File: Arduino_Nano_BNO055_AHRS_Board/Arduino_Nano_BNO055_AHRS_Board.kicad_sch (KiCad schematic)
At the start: 7 parts, among them J1 Conn_01x04, J2 Conn_01x02_Socket, J3 Conn_01x07_Pin, J4 Conn_01x02_Pin, J5 Conn_01x02_Pin, J6 Conn_01x06_Pin

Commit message: Made one update that I didn't save ...
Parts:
- removed J2: Conn_01x02_Socket, Connector_PinSocket_2.54mm:PinSocket_1x02_P2.54mm_Vertical, symbol Connector:Conn_01x02_Socket
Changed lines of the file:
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@@
   (junction (at 91.44 91.44) (diameter 0) (color 0 0 0 0)
   )
-  (junction (at 69.85 151.13) (diameter 0) (color 0 0 0 0)
-  )
-  (junction (at 80.01 130.81) (diameter 0) (color 0 0 0 0)
-  )
   (junction (at 92.71 130.81) (diameter 0) (color 0 0 0 0)
   )
@@
     (stroke (width 0) (type default))
   )
-  (wire (pts (xy 69.85 139.7) (xy 80.01 139.7))
-    (stroke (width 0) (type default))
-  )
-  (wire (pts (xy 50.8 130.81) (xy 80.01 130.81))
-    (stroke (width 0) (type default))
-  )
   (wire (pts (xy 130.81 91.44) (xy 147.32 91.44))
     (stroke (width 0) (type default))
@@
     (stroke (width 0) (type default))
   )
-  (wire (pts (xy 80.01 130.81) (xy 92.71 130.81))
+  (wire (pts (xy 50.8 130.81) (xy 92.71 130.81))
     (stroke (width 0) (type default))
   )
@@
     (stroke (width 0) (type default))
   )
-  (wire (pts (xy 59.69 151.13) (xy 69.85 151.13))
+  (wire (pts (xy 59.69 151.13) (xy 83.82 151.13))
     (stroke (width 0) (type default))
   )
@@
     (stroke (width 0) (type default))
   )
-  (wire (pts (xy 69.85 142.24) (xy 69.85 151.13))
-    (stroke (width 0) (type default))
-  )
   (wire (pts (xy 83.82 133.35) (xy 90.17 133.35))
     (stroke (width 0) (type default))
@@
     (stroke (width 0) (type default))
   )
-  (wire (pts (xy 80.01 139.7) (xy 80.01 130.81))
-    (stroke (width 0) (type default))
-  )
   (wire (pts (xy 30.48 88.9) (xy 30.48 124.46))
     (stroke (width 0) (type default))
@@
   )
   (wire (pts (xy 38.1 88.9) (xy 38.1 99.06))
-    (stroke (width 0) (type default))
-  )
-  (wire (pts (xy 69.85 151.13) (xy 83.82 151.13))
     (stroke (width 0) (type default))
   )
@@
         )
       )
-    )
-  )
-  (symbol (lib_id "Connector:Conn_01x02_Socket") (at 64.77 142.24 180) (unit 1)
-    (in_bom yes) (on_board yes) (dnp no) (fields_autoplaced)
-    (property "Reference" "J2" (at 65.405 135.89 0)
-      (effects (font (size 1.27 1.27)))
-    )
-    (property "Value" "Conn_01x02_Socket" (at 65.405 138.43 0)
-      (effects (font (size 1.27 1.27)))
-    )
-    (property "Footprint" "Connector_PinSocket_2.54mm:PinSocket_1x02_P2.54mm_Vertical" (at 64.77 142.24 0)
-      (effects (font (size 1.27 1.27)) hide)
-    )
-    (property "Datasheet" "~" (at 64.77 142.24 0)
-      (effects (font (size 1.27 1.27)) hide)
-    )
-    (pin "1")
-    (pin "2")
-    (instances
-      (project "Arduino_Nano_BNO055_AHRS_Board"
-        (path "/26c454b3-0fc6-4f29-b44e-9912b5b9bb77"
-          (reference "J2") (unit 1)
-        )
-      )

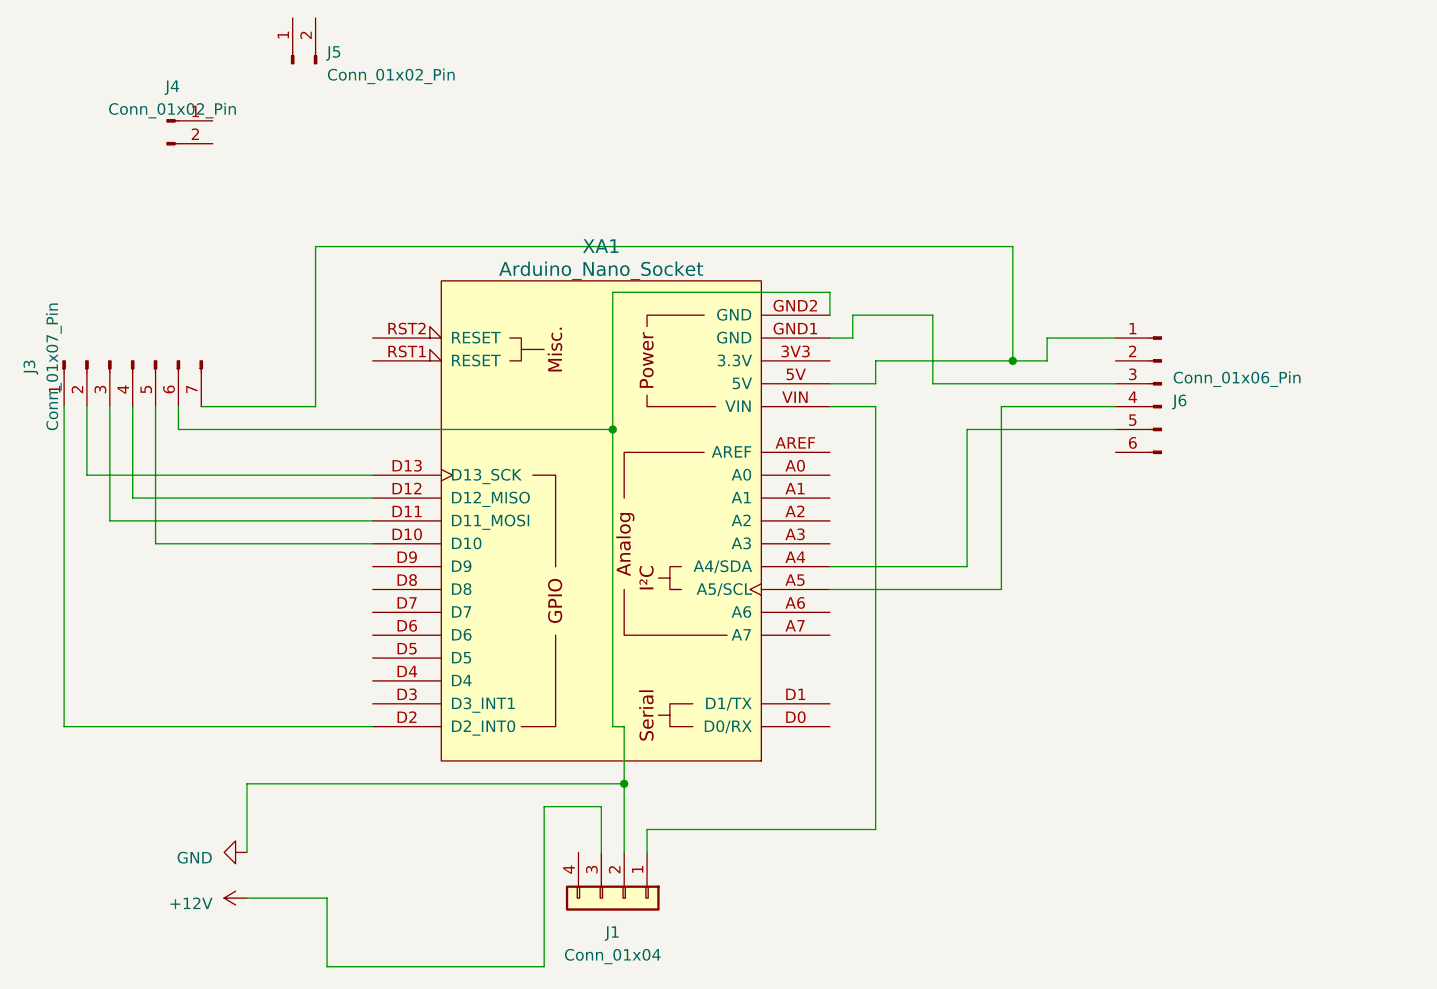
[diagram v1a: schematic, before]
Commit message: Updates Arduino_Nano_BNO055_AHRS_Board files. The older version required a via to cross two traces. This new version uses a larger PCB blank (one-sided) and no longer requires any vias. I also moved the BNO055 sensor away from the buck power converter (and all the other electronics on the board) to help minimize EMI, which can make it hard for the Magnetometer to calibrate.
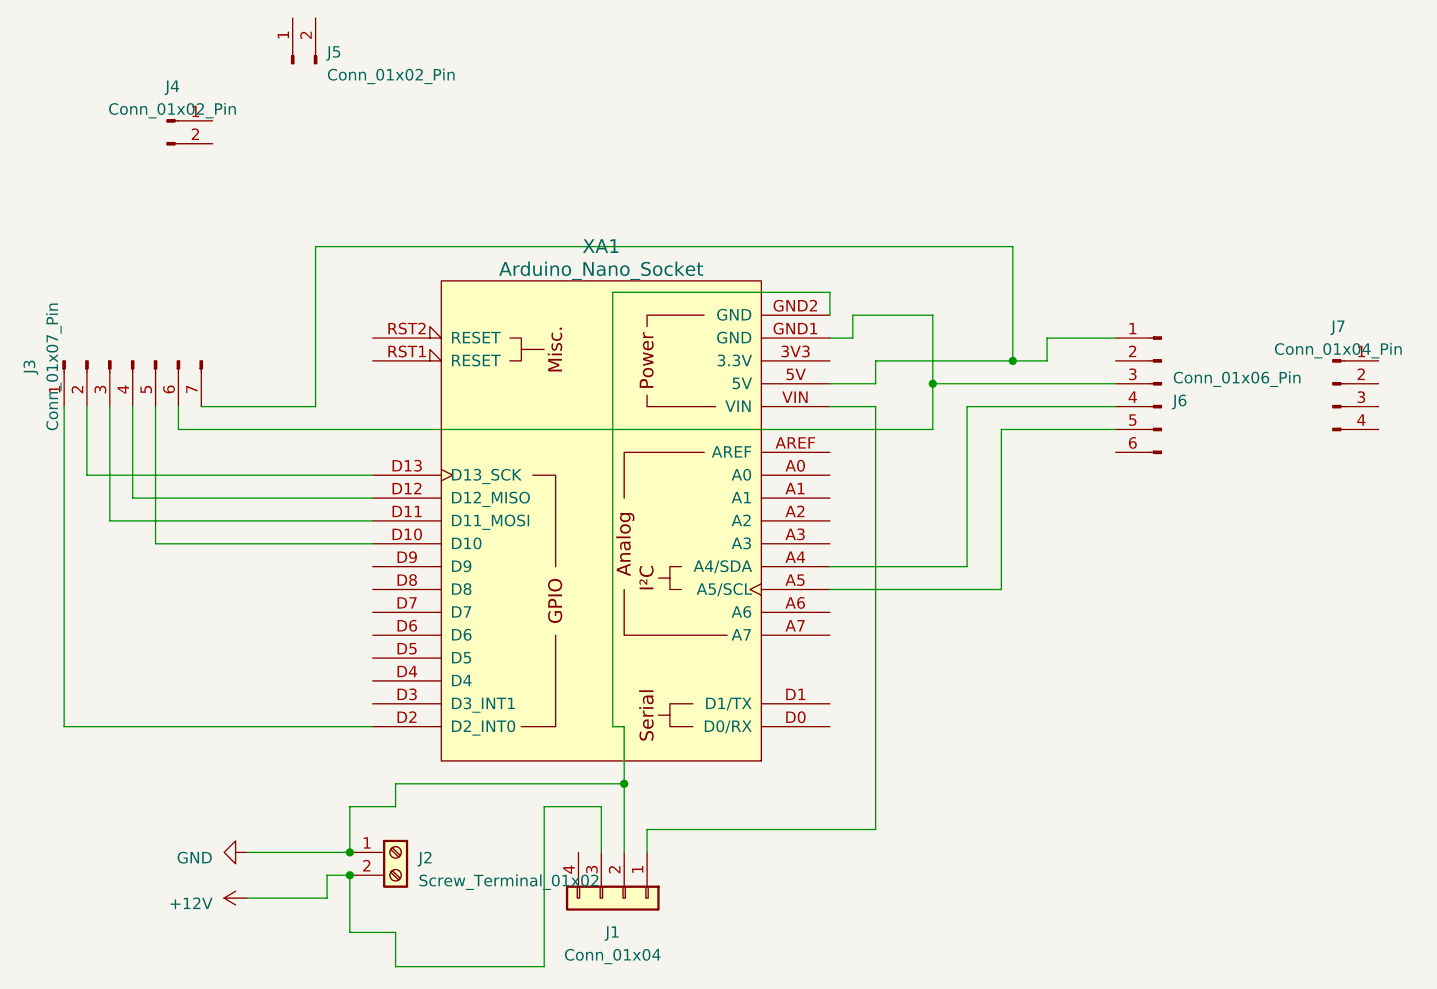
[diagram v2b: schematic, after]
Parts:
- added J2: Screw_Terminal_01x02, TerminalBlock:TerminalBlock_bornier-2_P5.08mm, symbol Connector:Screw_Terminal_01x02
- added J7: Conn_01x04_Pin, Connector_PinHeader_2.54mm:PinHeader_1x04_P2.54mm_Vertical, symbol Connector:Conn_01x04_Pin
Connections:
- net +12V: now also J2.2 (Pin_2)
- net GND: now also J2.1 (Pin_1); no longer J3.6 (Pin_6)
- net at XA1.A4 (A4/SDA): now also J6.4 (Pin_4); no longer J6.5 (Pin_5)
- net at XA1.A5 (A5/SCL): now also J6.5 (Pin_5); no longer J6.4 (Pin_4)
- net at J6.3 (Pin_3), XA1.GND1 (GND): now also J3.6 (Pin_6)
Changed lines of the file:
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@@
 (kicad_sch (version 20230121) (generator eeschema)
   (paper "A4")
-  (junction (at 91.44 91.44) (diameter 0) (color 0 0 0 0)
+  (junction (at 127 86.36) (diameter 0) (color 0 0 0 0)
+  )
+  (junction (at 62.23 140.97) (diameter 0) (color 0 0 0 0)
   )
   (junction (at 92.71 130.81) (diameter 0) (color 0 0 0 0)
   )
+  (junction (at 62.23 138.43) (diameter 0) (color 0 0 0 0)
+  )
   (junction (at 135.89 83.82) (diameter 0) (color 0 0 0 0)
   )
@@
     (stroke (width 0) (type default))
   )
-  (wire (pts (xy 50.8 138.43) (xy 50.8 130.81))
+  (wire (pts (xy 67.31 133.35) (xy 62.23 133.35))
     (stroke (width 0) (type default))
   )
@@
     (stroke (width 0) (type default))
   )
+  (wire (pts (xy 134.62 91.44) (xy 147.32 91.44))
+    (stroke (width 0) (type default))
+  )
   (wire (pts (xy 33.02 88.9) (xy 33.02 96.52))
     (stroke (width 0) (type default))
   )
+  (wire (pts (xy 127 91.44) (xy 127 86.36))
+    (stroke (width 0) (type default))
+  )
   (wire (pts (xy 83.82 133.35) (xy 83.82 151.13))
     (stroke (width 0) (type default))
   )
-  (wire (pts (xy 130.81 91.44) (xy 147.32 91.44))
+  (wire (pts (xy 67.31 130.81) (xy 67.31 133.35))
     (stroke (width 0) (type default))
   )
@@
     (stroke (width 0) (type default))
   )
+  (wire (pts (xy 50.8 138.43) (xy 62.23 138.43))
+    (stroke (width 0) (type default))
+  )
   (wire (pts (xy 115.57 86.36) (xy 120.65 86.36))
     (stroke (width 0) (type default))
   )
+  (wire (pts (xy 67.31 151.13) (xy 67.31 147.32))
+    (stroke (width 0) (type default))
+  )
   (wire (pts (xy 58.42 71.12) (xy 135.89 71.12))
     (stroke (width 0) (type default))
@@
     (stroke (width 0) (type default))
   )
+  (wire (pts (xy 59.69 140.97) (xy 62.23 140.97))
+    (stroke (width 0) (type default))
+  )
   (wire (pts (xy 35.56 88.9) (xy 35.56 101.6))
     (stroke (width 0) (type default))
   )
-  (wire (pts (xy 91.44 91.44) (xy 91.44 76.2))
-    (stroke (width 0) (type default))
-  )
-  (wire (pts (xy 50.8 130.81) (xy 92.71 130.81))
-    (stroke (width 0) (type default))
-  )
-  (wire (pts (xy 130.81 106.68) (xy 130.81 91.44))
+  (wire (pts (xy 91.44 76.2) (xy 91.44 124.46))
+    (stroke (width 0) (type default))
+  )
+  (wire (pts (xy 130.81 88.9) (xy 130.81 106.68))
+    (stroke (width 0) (type default))
+  )
+  (wire (pts (xy 62.23 147.32) (xy 62.23 140.97))
     (stroke (width 0) (type default))
   )
@@
     (stroke (width 0) (type default))
   )
+  (wire (pts (xy 67.31 130.81) (xy 92.71 130.81))
+    (stroke (width 0) (type default))
+  )
   (wire (pts (xy 43.18 88.9) (xy 43.18 91.44))
     (stroke (width 0) (type default))
   )
+  (wire (pts (xy 59.69 143.51) (xy 59.69 140.97))
+    (stroke (width 0) (type default))
+  )
   (wire (pts (xy 120.65 135.89) (xy 120.65 88.9))
     (stroke (width 0) (type default))
   )
-  (wire (pts (xy 134.62 88.9) (xy 147.32 88.9))
-    (stroke (width 0) (type default))
-  )
-  (wire (pts (xy 59.69 151.13) (xy 83.82 151.13))
+  (wire (pts (xy 67.31 151.13) (xy 83.82 151.13))
     (stroke (width 0) (type default))
   )
@@
     (stroke (width 0) (type default))
   )
+  (wire (pts (xy 67.31 147.32) (xy 62.23 147.32))
+    (stroke (width 0) (type default))
+  )
+  (wire (pts (xy 134.62 91.44) (xy 134.62 109.22))
+    (stroke (width 0) (type default))
+  )
   (wire (pts (xy 83.82 133.35) (xy 90.17 133.35))
     (stroke (width 0) (type default))
@@
     (stroke (width 0) (type default))
   )
-  (wire (pts (xy 134.62 109.22) (xy 134.62 88.9))
+  (wire (pts (xy 43.18 91.44) (xy 127 91.44))
+    (stroke (width 0) (type default))
+  )
+  (wire (pts (xy 130.81 88.9) (xy 147.32 88.9))
     (stroke (width 0) (type default))
   )
@@
     (stroke (width 0) (type default))
   )
-  (wire (pts (xy 91.44 124.46) (xy 91.44 91.44))
-    (stroke (width 0) (type default))
-  )
   (wire (pts (xy 92.71 130.81) (xy 92.71 138.43))
     (stroke (width 0) (type default))
   )
-  (wire (pts (xy 43.18 91.44) (xy 91.44 91.44))
-    (stroke (width 0) (type default))
-  )
   (wire (pts (xy 40.64 88.9) (xy 40.64 104.14))
     (stroke (width 0) (type default))
@@
     (stroke (width 0) (type default))
   )
-  (wire (pts (xy 59.69 143.51) (xy 59.69 151.13))
-    (stroke (width 0) (type default))
-  )
   (wire (pts (xy 127 86.36) (xy 147.32 86.36))
     (stroke (width 0) (type default))
   )
   (wire (pts (xy 38.1 88.9) (xy 38.1 99.06))
+    (stroke (width 0) (type default))
+  )
+  (wire (pts (xy 62.23 133.35) (xy 62.23 138.43))
     (stroke (width 0) (type default))
   )
@@
     )
   )
+  (symbol (lib_id "Connector:Conn_01x04_Pin") (at 171.45 86.36 0) (unit 1)
+    (in_bom yes) (on_board yes) (dnp no) (fields_autoplaced)
+    (property "Reference" "J7" (at 172.085 80.01 0)
+      (effects (font (size 1.27 1.27)))
+    )
+    (property "Value" "Conn_01x04_Pin" (at 172.085 82.55 0)
+      (effects (font (size 1.27 1.27)))
+    )
+    (property "Footprint" "Connector_PinHeader_2.54mm:PinHeader_1x04_P2.54mm_Vertical" (at 171.45 86.36 0)
+      (effects (font (size 1.27 1.27)) hide)
+    )
+    (property "Datasheet" "~" (at 171.45 86.36 0)
+      (effects (font (size 1.27 1.27)) hide)
+    )
+    (pin "1")
+    (pin "2")
+    (pin "3")
+    (pin "4")
+    (instances
+      (project "Arduino_Nano_BNO055_AHRS_Board"
+        (path "/26c454b3-0fc6-4f29-b44e-9912b5b9bb77"
+          (reference "J7") (unit 1)
+        )
+      )
+    )
+  )
   (symbol (lib_id "power:GND") (at 50.8 138.43 270) (unit 1)
     (in_bom yes) (on_board yes) (dnp no) (fields_autoplaced)
@@
         )
       )
+    )
+  )
+  (symbol (lib_id "Connector:Screw_Terminal_01x02") (at 67.31 138.43 0) (unit 1)
+    (in_bom yes) (on_board yes) (dnp no) (fields_autoplaced)
+    (property "Reference" "J2" (at 69.85 139.065 0)
+      (effects (font (size 1.27 1.27)) (justify left))
+    )
+    (property "Value" "Screw_Terminal_01x02" (at 69.85 141.605 0)
+      (effects (font (size 1.27 1.27)) (justify left))
+    )
+    (property "Footprint" "TerminalBlock:TerminalBlock_bornier-2_P5.08mm" (at 67.31 138.43 0)
+      (effects (font (size 1.27 1.27)) hide)
+    )
+    (property "Datasheet" "~" (at 67.31 138.43 0)
+      (effects (font (size 1.27 1.27)) hide)
+    )
+    (pin "1")
+    (pin "2")
+    (instances
+      (project "Arduino_Nano_BNO055_AHRS_Board"
+        (path "/26c454b3-0fc6-4f29-b44e-9912b5b9bb77"
+          (reference "J2") (unit 1)
+        )
+      )
